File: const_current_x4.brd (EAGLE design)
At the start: 86.7 x 55.2 mm, 22 parts

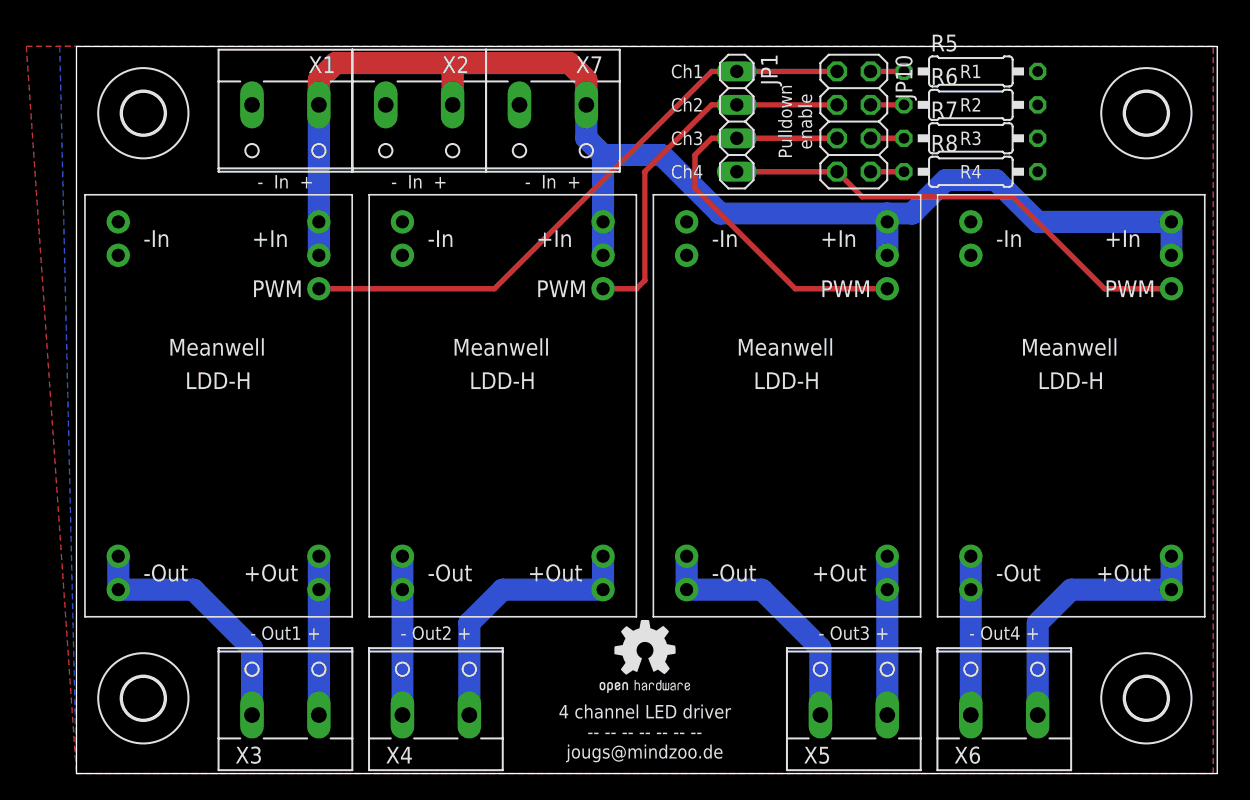
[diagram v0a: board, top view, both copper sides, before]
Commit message: Fixed bug in routing of Out- for the constant current modules
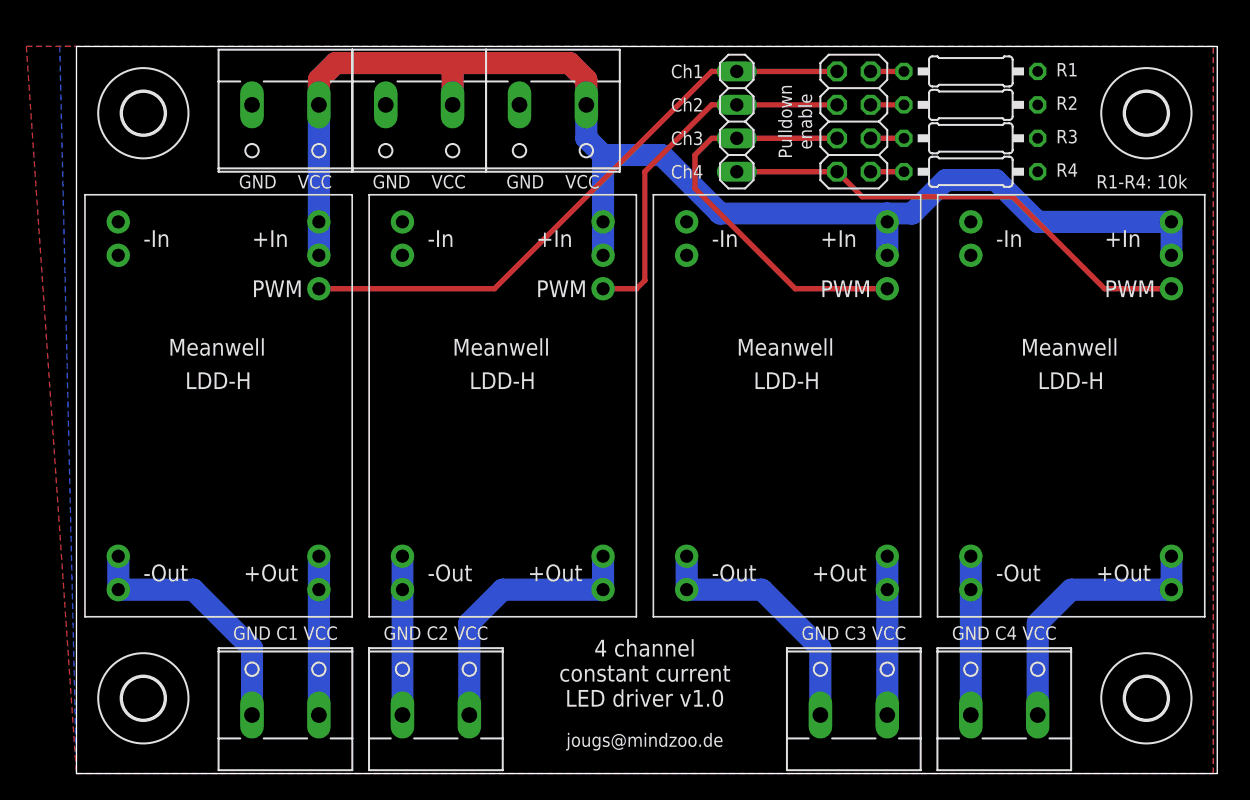
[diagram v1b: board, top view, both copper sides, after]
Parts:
- removed U$1: (no value), NBitWonder:OSHW2
- renumbered R5 to R1, R6 to R2, R7 to R3, R8 to R4
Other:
- board text added: "4 channel constant current LED driver v1.0"
- board text added: "GND C1 VCC"
- board text added: "GND C2 VCC"
- board text added: "GND C3 VCC"
- board text added: "GND C4 VCC"
- board text added: "GND VCC"
- board text added: "R1-R4: 10k"
- board text added: "jougs@mindzoo.de"
- board text removed: "- In +"
- board text removed: "- Out1 +"
- board text removed: "- Out2 +"
- board text removed: "- Out3 +"
- board text removed: "- Out4 +"
- board text removed: "4 channel LED driver -- -- -- -- -- -- -- jougs@mindzoo.de"
- board text removed: "R1"
- board text removed: "R2"
- board text removed: "R3"
- board text removed: "R4"
